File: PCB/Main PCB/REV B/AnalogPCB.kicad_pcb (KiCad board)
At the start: 2 copper layers, 60 x 100 mm, 60 parts, among them J1 DF12NB_4.0_-20DP-0.5V_51_, J2 393570002, J3 393570002, J4 393570002, J5 393570002, J6 SJ3-35053D, Q1 2N7002, Q2 2N7002, Q3 2N7002, U1 ALDP105W, U2 ALDP105W, U3 ALDP105W

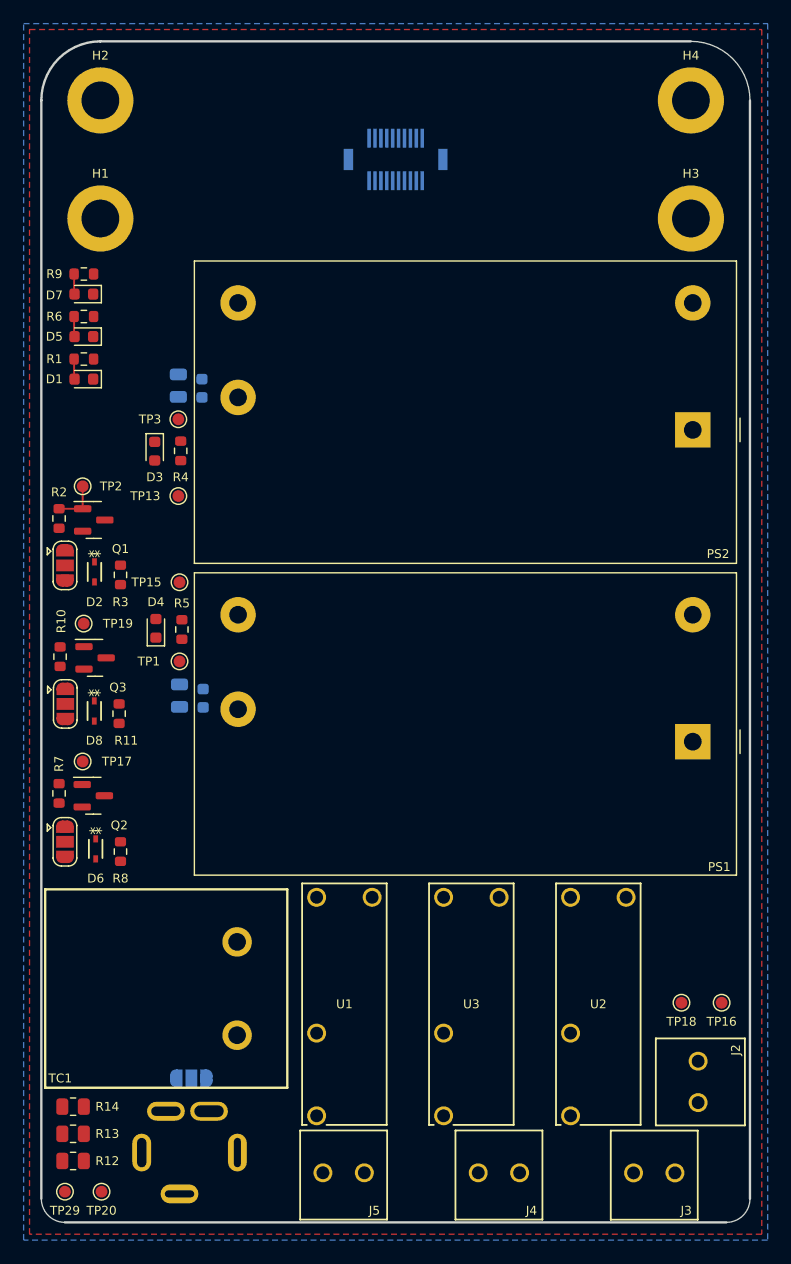
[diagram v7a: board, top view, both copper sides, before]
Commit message: PCB - Analog AC routing first pass
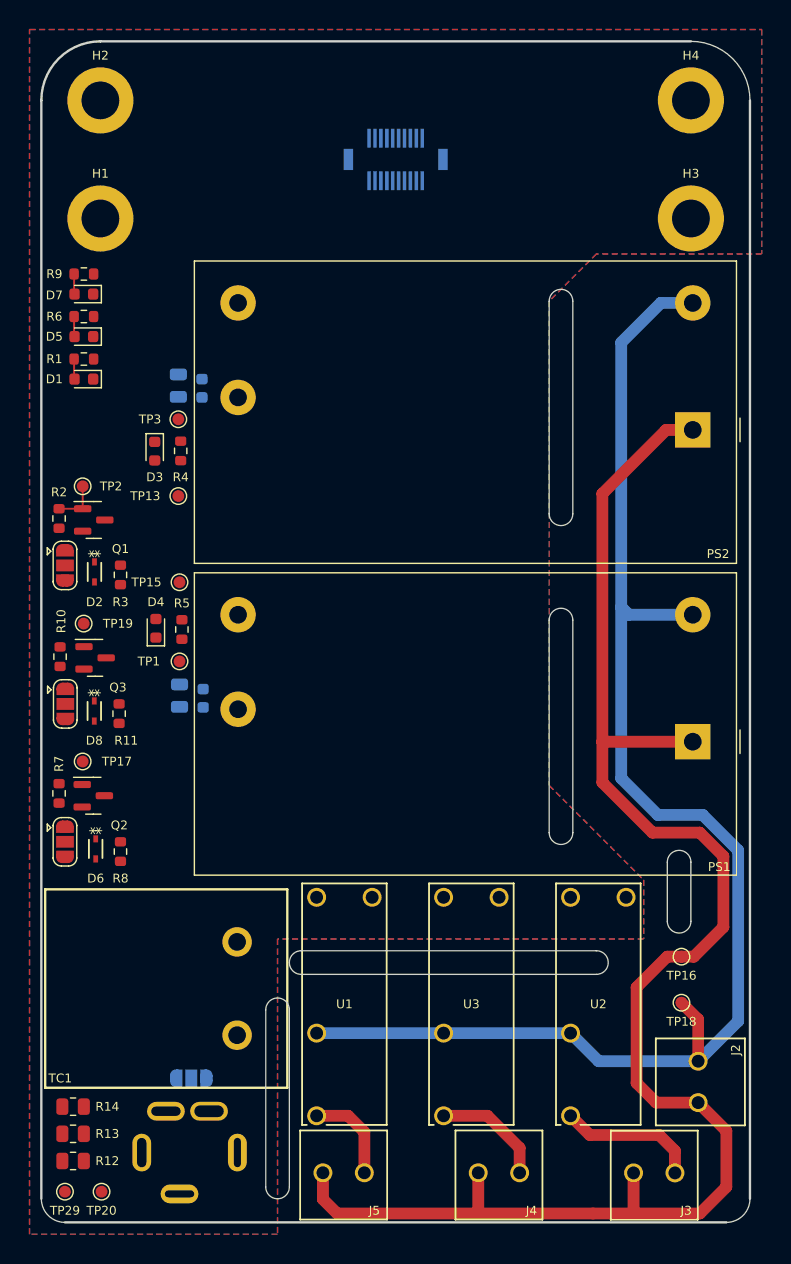
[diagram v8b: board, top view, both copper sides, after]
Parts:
- moved TP16 5.17 mm to (104.2, 127.5)
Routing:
- net /AC_N: track 0.00 -> 137.2 mm
- net /AC_L: track 0.00 -> 121.2 mm
- net /Ignitor_+: track 0.00 -> 11.9 mm
- net /Fan_+: track 0.00 -> 9.67 mm
- net /Auger_+: track 0.00 -> 8.06 mm
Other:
- outline, holes or cut-outs redrawn
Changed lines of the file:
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@@
   )
   (footprint "TestPoint:TestPoint_Pad_D1.0mm" (layer "F.Cu")
-    (at 107.6 131.4 -90)
+    (at 104.2 127.5 -90)
     (descr "SMD pad as test Point, diameter 1.0mm")
     (tags "test point SMD pad")
@@
     )
   )
+  (gr_arc (start 95 90) (mid 94 91) (end 93 90) (layer "Edge.Cuts") (width 0.1))
+  (gr_line (start 95 99) (end 95 117) (layer "Edge.Cuts") (width 0.1))
   (gr_arc locked (start 105 50) (mid 108.535534 51.464466) (end 110 55) (layer "Edge.Cuts") (width 0.1))
+  (gr_line (start 69 147) (end 69 132) (layer "Edge.Cuts") (width 0.1))
   (gr_arc (start 110 148) (mid 109.414214 149.414214) (end 108 150) (layer "Edge.Cuts") (width 0.1))
   (gr_line locked (start 105 50) (end 55 50) (layer "Edge.Cuts") (width 0.2))
+  (gr_line (start 71 132) (end 71 147) (layer "Edge.Cuts") (width 0.1))
+  (gr_line (start 97 129) (end 72 129) (layer "Edge.Cuts") (width 0.1))
+  (gr_line (start 95 72) (end 95 90) (layer "Edge.Cuts") (width 0.1))
   (gr_arc locked (start 50 55) (mid 51.464466 51.464466) (end 55 50) (layer "Edge.Cuts") (width 0.2))
+  (gr_arc (start 95 117) (mid 94 118) (end 93 117) (layer "Edge.Cuts") (width 0.1))
+  (gr_arc (start 97 127) (mid 98 128) (end 97 129) (layer "Edge.Cuts") (width 0.1))
+  (gr_arc (start 93 99) (mid 94 98) (end 95 99) (layer "Edge.Cuts") (width 0.1))
+  (gr_arc (start 93 72) (mid 94 71) (end 95 72) (layer "Edge.Cuts") (width 0.1))
   (gr_line locked (start 52 150) (end 108 150) (layer "Edge.Cuts") (width 0.2))
+  (gr_arc (start 103 119.5) (mid 104 118.5) (end 105 119.5) (layer "Edge.Cuts") (width 0.1))
+  (gr_arc (start 72 129) (mid 71 128) (end 72 127) (layer "Edge.Cuts") (width 0.1))
+  (gr_line (start 105 119.5) (end 105 124.5) (layer "Edge.Cuts") (width 0.1))
+  (gr_arc (start 69 132) (mid 70 131) (end 71 132) (layer "Edge.Cuts") (width 0.1))
   (gr_arc (start 52 150) (mid 50.585786 149.414214) (end 50 148) (layer "Edge.Cuts") (width 0.1))
   (gr_line locked (start 110 148) (end 110 55) (layer "Edge.Cuts") (width 0.2))
+  (gr_line (start 72 127) (end 97 127) (layer "Edge.Cuts") (width 0.1))
+  (gr_arc (start 105 124.5) (mid 104 125.5) (end 103 124.5) (layer "Edge.Cuts") (width 0.1))
   (gr_line locked (start 50 55) (end 50 148) (layer "Edge.Cuts") (width 0.2))
+  (gr_line (start 103 119.5) (end 103 124.5) (layer "Edge.Cuts") (width 0.1))
+  (gr_line (start 93 90) (end 93 72) (layer "Edge.Cuts") (width 0.1))
+  (gr_arc (start 71 147) (mid 70 148) (end 69 147) (layer "Edge.Cuts") (width 0.1))
+  (gr_line (start 93 117) (end 93 99) (layer "Edge.Cuts") (width 0.1))
   (segment (start 52.775 69.7) (end 52.775 71.3625) (width 0.16) (layer "F.Cu") (net 7))
   (segment (start 52.775 71.3625) (end 52.8125 71.4) (width 0.16) (layer "F.Cu") (net 7))
@@
   (segment (start 52.775 74.9625) (end 52.8125 75) (width 0.16) (layer "F.Cu") (net 12))
   (segment (start 52.775 73.3) (end 52.775 74.9625) (width 0.16) (layer "F.Cu") (net 12))
+  (segment (start 105.6095 136.3523) (end 105.6095 132.8095) (width 1) (layer "F.Cu") (net 14))
+  (segment (start 105.6095 132.8095) (end 104.2 131.4) (width 1) (layer "F.Cu") (net 14))
+  (segment (start 99.1 97.9) (end 99.1 75.5) (width 1) (layer "B.Cu") (net 14))
+  (segment (start 94.80975 133.974951) (end 73.30975 133.974951) (width 1) (layer "B.Cu") (net 14))
+  (segment (start 99.75 98.55) (end 99.1 97.9) (width 1) (layer "B.Cu") (net 14))
+  (segment (start 97.187099 136.3523) (end 94.80975 133.974951) (width 1) (layer "B.Cu") (net 14))
+  (segment (start 99.1 75.5) (end 102.45 72.15) (width 1) (layer "B.Cu") (net 14))
+  (segment (start 105.6095 136.3523) (end 97.187099 136.3523) (width 1) (layer "B.Cu") (net 14))
+  (segment (start 102.2 115.5) (end 106 115.5) (width 1) (layer "B.Cu") (net 14))
+  (segment (start 99.1 97.9) (end 99.1 112.4) (width 1) (layer "B.Cu") (net 14))
+  (segment (start 99.1 112.4) (end 102.2 115.5) (width 1) (layer "B.Cu") (net 14))
+  (segment (start 102.45 72.15) (end 105.1575 72.15) (width 1) (layer "B.Cu") (net 14))
+  (segment (start 106 115.5) (end 109 118.5) (width 1) (layer "B.Cu") (net 14))
+  (segment (start 109 132.9618) (end 105.6095 136.3523) (width 1) (layer "B.Cu") (net 14))
+  (segment (start 105.1575 98.55) (end 99.75 98.55) (width 1) (layer "B.Cu") (net 14))
+  (segment (start 109 118.5) (end 109 132.9618) (width 1) (layer "B.Cu") (net 14))
+  (segment (start 108 147) (end 105.754 149.246) (width 1) (layer "F.Cu") (net 15))
+  (segment (start 87.054 149.246) (end 75.046 149.246) (width 1) (layer "F.Cu") (net 15))
+  (segment (start 101.75 117) (end 105.75 117) (width 1) (layer "F.Cu") (net 15))
+  (segment (start 105.754 149.246) (end 100.146 149.246) (width 1) (layer "F.Cu") (net 15))
+  (segment (start 105.6095 139.8575) (end 102.0575 139.8575) (width 1) (layer "F.Cu") (net 15))
+  (segment (start 105.1575 109.3) (end 97.5 109.3) (width 1) (layer "F.Cu") (net 15))
+  (segment (start 102.9 82.9) (end 105.1575 82.9) (width 1) (layer "F.Cu") (net 15))
+  (segment (start 75.046 149.246) (end 73.8425 148.0425) (width 1) (layer "F.Cu") (net 15))
+  (segment (start 103 127.5) (end 104.2 127.5) (width 1) (layer "F.Cu") (net 15))
+  (segment (start 73.8425 148.0425) (end 73.8425 145.8) (width 1) (layer "F.Cu") (net 15))
+  (segment (start 107.75 125) (end 105.25 127.5) (width 1) (layer "F.Cu") (net 15))
+  (segment (start 105.75 117) (end 107.75 119) (width 1) (layer "F.Cu") (net 15))
+  (segment (start 100.4 130.1) (end 103 127.5) (width 1) (layer "F.Cu") (net 15))
+  (segment (start 97.5 109.3) (end 97.5 112.75) (width 1) (layer "F.Cu") (net 15))
+  (segment (start 102.0575 139.8575) (end 100.4 138.2) (width 1) (layer "F.Cu") (net 15))
+  (segment (start 100.1425 149.2425) (end 100.146 149.246) (width 1) (layer "F.Cu") (net 15))
+  (segment (start 100.4 138.2) (end 100.4 130.1) (width 1) (layer "F.Cu") (net 15))
+  (segment (start 107.75 119) (end 107.75 125) (width 1) (layer "F.Cu") (net 15))
+  (segment (start 96.706 149.246) (end 87.054 149.246) (width 1) (layer "F.Cu") (net 15))
+  (segment (start 105.6095 139.8575) (end 108 142.248) (width 1) (layer "F.Cu") (net 15))
+  (segment (start 97.5 112.75) (end 101.75 117) (width 1) (layer "F.Cu") (net 15))
+  (segment (start 100.146 149.246) (end 96.706 149.246) (width 1) (layer "F.Cu") (net 15))
+  (segment (start 97.5 109.3) (end 97.5 88.3) (width 1) (layer "F.Cu") (net 15))
+  (segment (start 108 142.248) (end 108 147) (width 1) (layer "F.Cu") (net 15))
+  (segment (start 86.9925 145.8) (end 86.9925 149.1845) (width 1) (layer "F.Cu") (net 15))
+  (segment (start 97.5 88.3) (end 102.9 82.9) (width 1) (layer "F.Cu") (net 15))
+  (segment (start 86.9925 149.1845) (end 87.054 149.246) (width 1) (layer "F.Cu") (net 15))
+  (segment (start 100.1425 145.8095) (end 100.1425 149.2425) (width 1) (layer "F.Cu") (net 15))
+  (segment (start 105.25 127.5) (end 104.2 127.5) (width 1) (layer "F.Cu") (net 15))
+  (segment (start 73.30975 140.97495) (end 75.97495 140.97495) (width 1) (layer "F.Cu") (net 16))
+  (segment (start 75.97495 140.97495) (end 77.3477 142.3477) (width 1) (layer "F.Cu") (net 16))
+  (segment (start 77.3477 142.3477) (end 77.3477 145.8) (width 1) (layer "F.Cu") (net 16))
+  (segment (start 90.4977 145.8) (end 90.4977 143.6977) (width 1) (layer "F.Cu") (net 17))
+  (segment (start 87.77495 140.97495) (end 84.05975 140.97495) (width 1) (layer "F.Cu") (net 17))
+  (segment (start 90.4977 143.6977) (end 87.77495 140.97495) (width 1) (layer "F.Cu") (net 17))
+  (segment (start 103.6477 143.9477) (end 102.3 142.6) (width 1) (layer "F.Cu") (net 18))
+  (segment (start 103.6477 145.8095) (end 103.6477 143.9477) (width 1) (layer "F.Cu") (net 18))
+  (segment (start 102.3 142.6) (end 96.4348 142.6) (width 1) (layer "F.Cu") (net 18))
+  (segment (start 96.4348 142.6) (end 94.80975 140.97495) (width 1) (layer "F.Cu") (net 18))
   (segment (start 53.5 89.575) (end 53.5 87.675) (width 0.16) (layer "F.Cu") (net 22))
   (segment (start 53.5 89.575) (end 51.5 89.575) (width 0.16) (layer "F.Cu") (net 22))
-  (zone (net 1) (net_name "GND") (layer "F.Cu") (hatch edge 0.508)
+  (zone (net 1) (net_name "GND") (layers F&B.Cu) (hatch edge 0.508)
     (connect_pads (clearance 0.508))
     (min_thickness 0.254) (filled_areas_thickness no)
@@
     (polygon
       (pts
-        (xy 111 151)
+        (xy 111 68)
+        (xy 97 68)
+        (xy 93 72)
+        (xy 93 113)
+        (xy 101 121)
+        (xy 101 126)
+        (xy 70 126)
+        (xy 70 151)
         (xy 49 151)
         (xy 49 49)
@@
       )
     )
-  )
-  (zone (net 1) (net_name "GND") (layer "B.Cu") (hatch edge 0.508)
-    (connect_pads (clearance 0.508))
-    (min_thickness 0.254) (filled_areas_thickness no)
-    (fill yes (thermal_gap 0.508) (thermal_bridge_width 0.508) (smoothing fillet) (radius 1))
-    (polygon
-      (pts
-        (xy 111.5 151.5)
-        (xy 48.5 151.5)
-        (xy 48.5 48.5)
-        (xy 111.5 48.5)
-      )
-    )
